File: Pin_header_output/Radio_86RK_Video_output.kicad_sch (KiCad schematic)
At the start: 9 parts, among them J1 Conn_01x05, Q1 2N3904

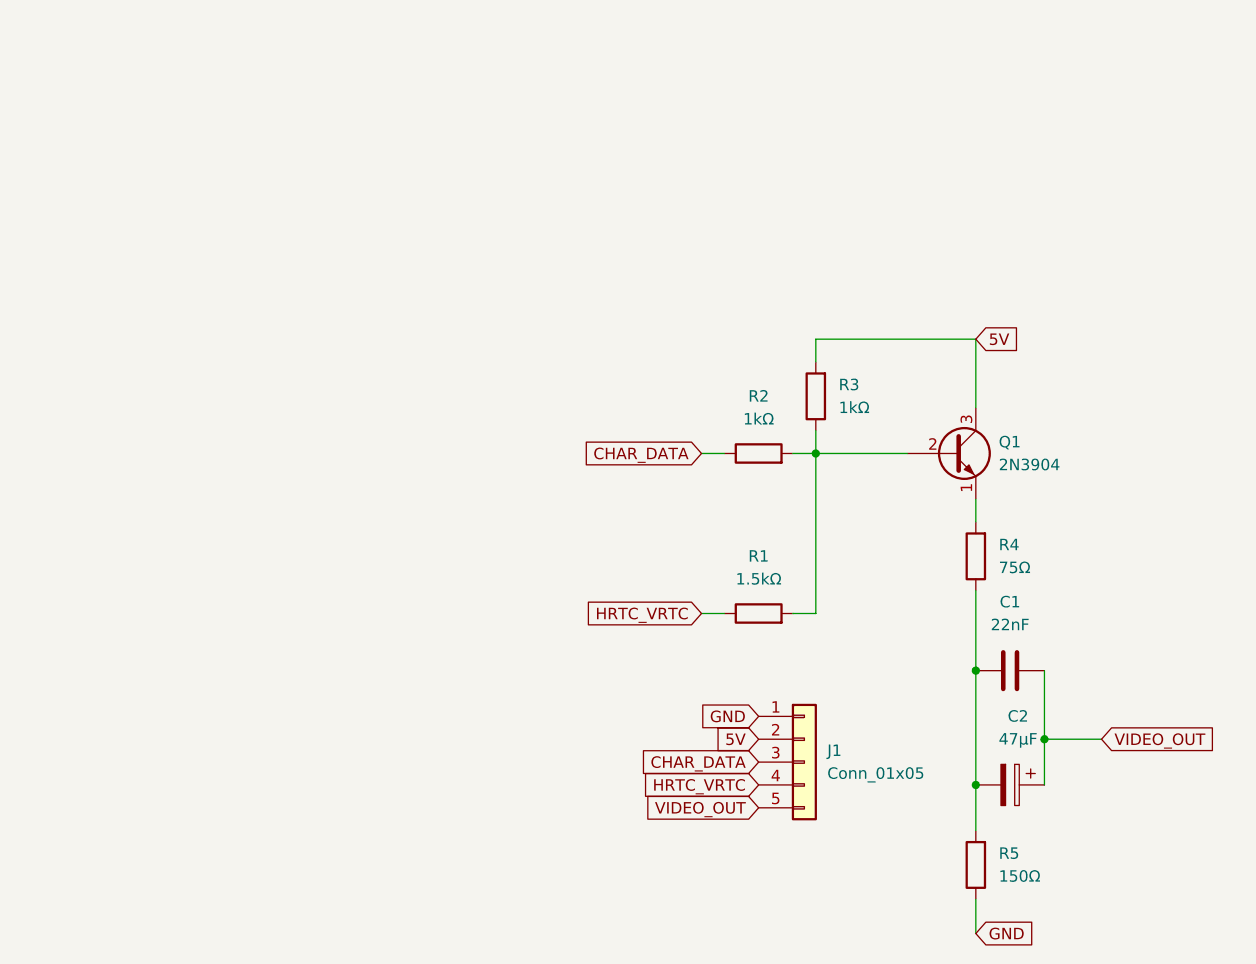
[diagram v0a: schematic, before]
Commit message: Added mounting hole
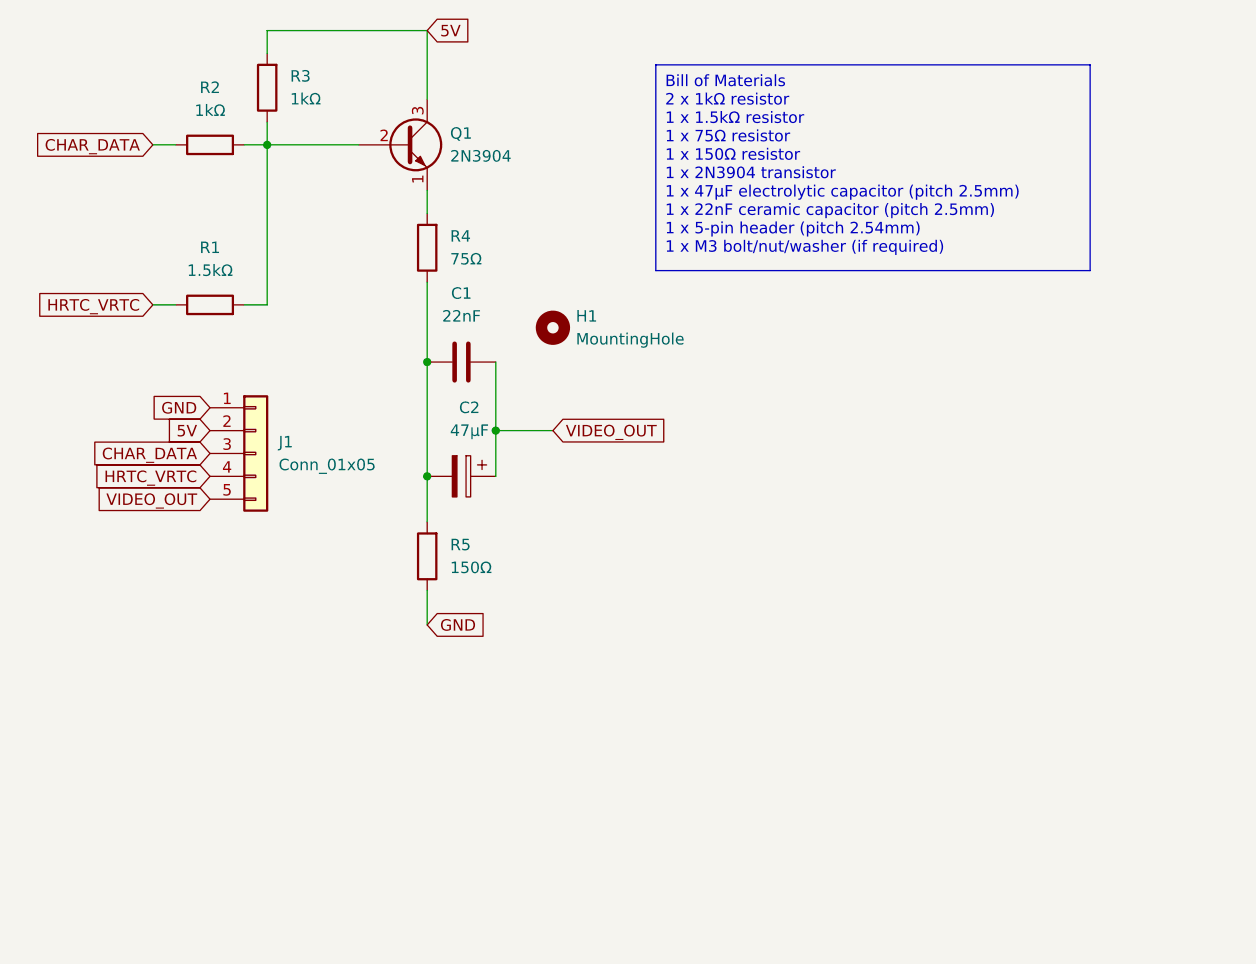
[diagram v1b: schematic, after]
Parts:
- added H1: MountingHole, MountingHole:MountingHole_3.2mm_M3, symbol Mechanical:MountingHole
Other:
- moved on the sheet: C1, C2, J1, Q1, R1, R2, R3, R4, R5
